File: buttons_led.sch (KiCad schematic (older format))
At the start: 13 parts, among them Q1201 2N7002P, SW1201 SW_Push, SW1202 SW_Push, SW1203 SW_Push, SW1204 SW_Push, SW1205 SW_Push

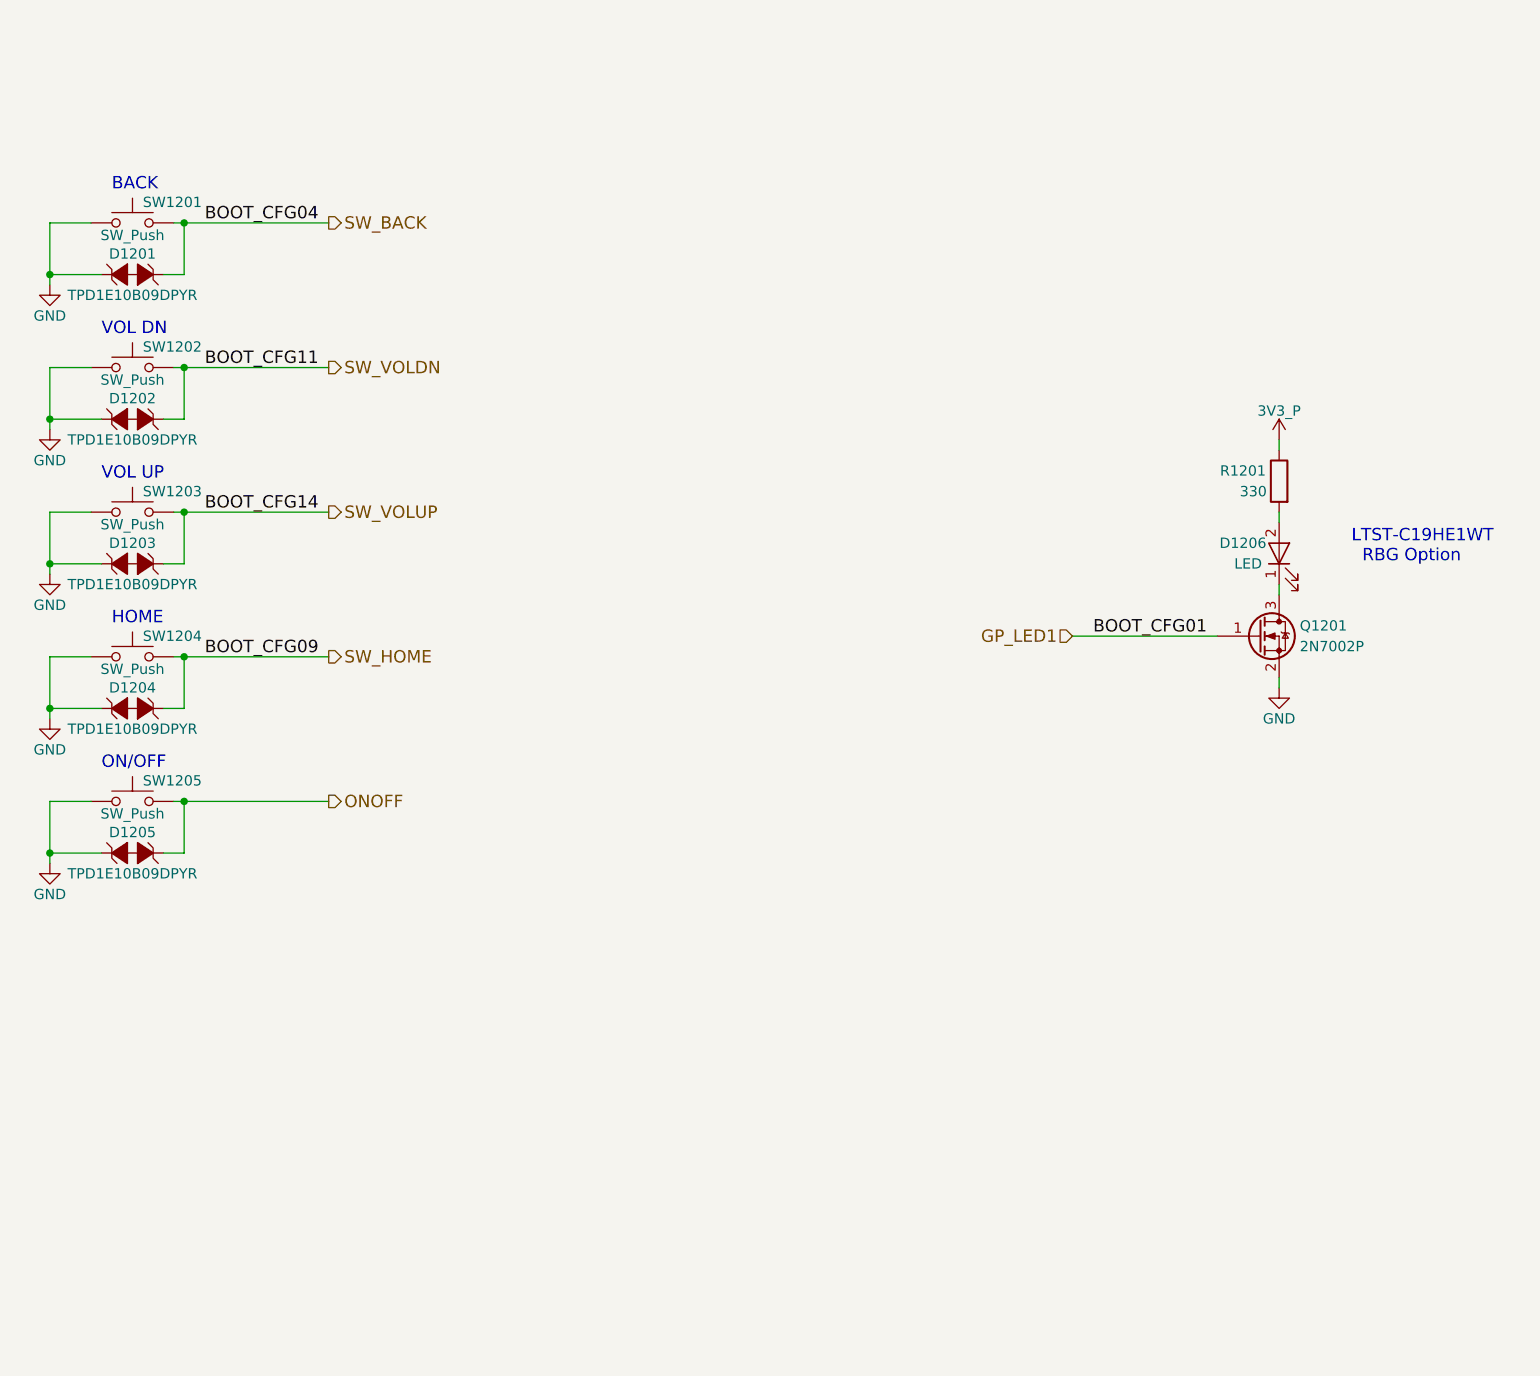
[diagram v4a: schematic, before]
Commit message: Add USB type C circuit with DRP PD capability, should sink near 2A @ 5-6.5V and source 550mA @ 5V
Removed the reverse current protection circuit from the last commit due to the requirement changing to only 18650 battery and USB-C being possible power sources

Next thing to add is the charging circuit when the USB-C is in sink mode/role
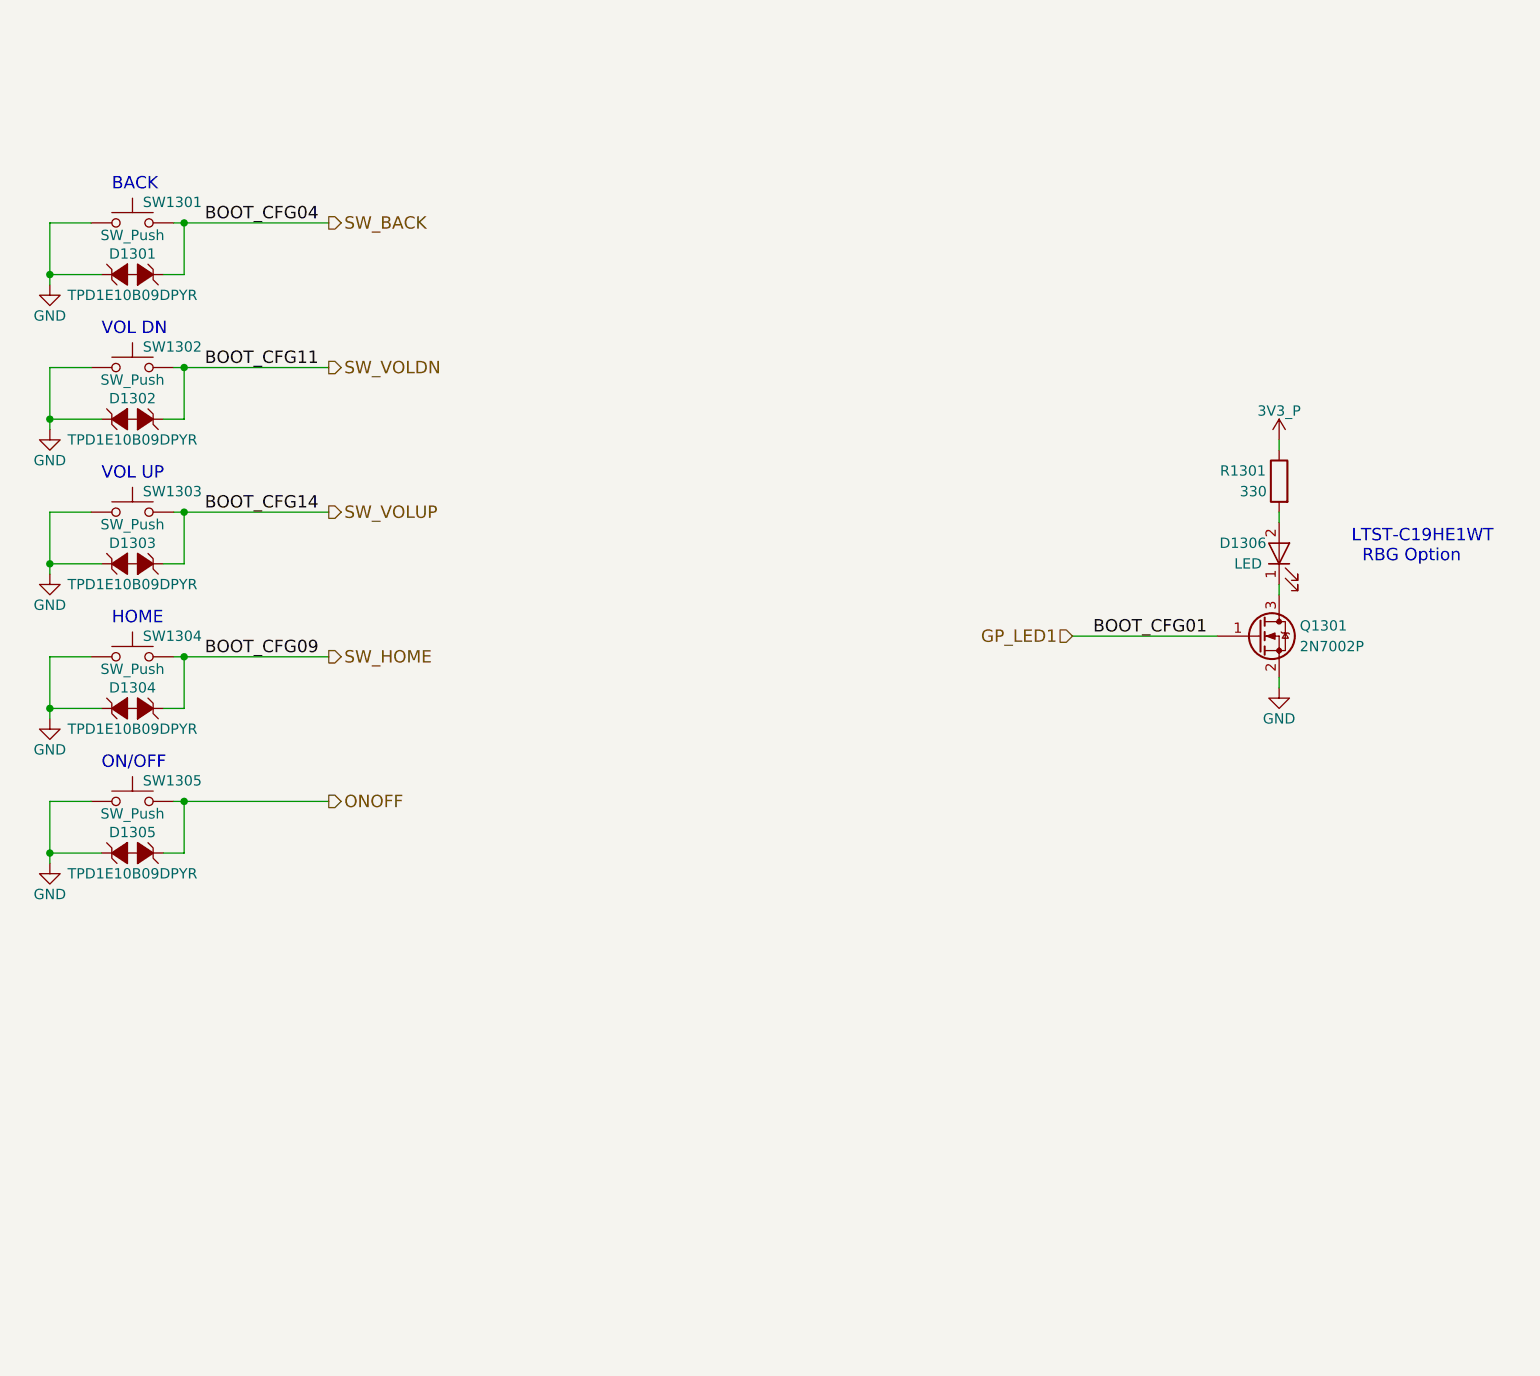
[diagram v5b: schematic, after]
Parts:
- renumbered D1201 to D1301, D1202 to D1302, D1203 to D1303, D1204 to D1304, D1205 to D1305, D1206 to D1306, Q1201 to Q1301, R1201 to R1301, SW1201 to SW1301, SW1202 to SW1302, SW1203 to SW1303, SW1204 to SW1304, SW1205 to SW1305
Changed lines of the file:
@@
 $Descr A4 11693 8268
 encoding utf-8
-Sheet 12 14
+Sheet 13 15
 Title "Buttons & LED"
-Date "2018-04-18"
+Date "2018-04-19"
 Rev "v0.1.0"
 Comp "Purism SPC"
@@
 $EndDescr
 $Comp
-L SW_Push SW1201
+L SW_Push SW1301
 U 1 1 5ACC398C
 P 3200 1700
-F 0 "SW1201" H 3250 1800 50  0000 L CNN
+F 0 "SW1301" H 3250 1800 50  0000 L CNN
 F 1 "SW_Push" H 3200 1640 50  0000 C CNN
 F 2 "" H 3200 1900 50  0001 C CNN
@@
 $EndComp
 $Comp
-L SW_Push SW1202
+L SW_Push SW1302
 U 1 1 5ACC39A6
 P 3200 2400
-F 0 "SW1202" H 3250 2500 50  0000 L CNN
+F 0 "SW1302" H 3250 2500 50  0000 L CNN
 F 1 "SW_Push" H 3200 2340 50  0000 C CNN
 F 2 "" H 3200 2600 50  0001 C CNN
@@
 $EndComp
 $Comp
-L SW_Push SW1203
+L SW_Push SW1303
 U 1 1 5ACC3A06
 P 3200 3100
-F 0 "SW1203" H 3250 3200 50  0000 L CNN
+F 0 "SW1303" H 3250 3200 50  0000 L CNN
 F 1 "SW_Push" H 3200 3040 50  0000 C CNN
 F 2 "" H 3200 3300 50  0001 C CNN
@@
 $EndComp
 $Comp
-L SW_Push SW1204
+L SW_Push SW1304
 U 1 1 5ACC3A3E
 P 3200 3800
-F 0 "SW1204" H 3250 3900 50  0000 L CNN
+F 0 "SW1304" H 3250 3900 50  0000 L CNN
 F 1 "SW_Push" H 3200 3740 50  0000 C CNN
 F 2 "" H 3200 4000 50  0001 C CNN
@@
 $EndComp
 $Comp
-L SW_Push SW1205
+L SW_Push SW1305
 U 1 1 5ACC3AC2
 P 3200 4500
-F 0 "SW1205" H 3250 4600 50  0000 L CNN
+F 0 "SW1305" H 3250 4600 50  0000 L CNN
 F 1 "SW_Push" H 3200 4440 50  0000 C CNN
 F 2 "" H 3200 4700 50  0001 C CNN
@@
 $EndComp
 $Comp
-L TVS_DIODE D1201
+L TVS_DIODE D1301
 U 1 1 5ACC3B61
 P 3200 1950
-F 0 "D1201" H 3200 2050 50  0000 C CNN
+F 0 "D1301" H 3200 2050 50  0000 C CNN
 F 1 "TPD1E10B09DPYR" H 3200 1850 50  0000 C CNN
 F 2 "" H 3300 1950 50  0001 C CNN
@@
 $EndComp
 $Comp
-L TVS_DIODE D1202
+L TVS_DIODE D1302
 U 1 1 5ACC3BD8
 P 3200 2650
-F 0 "D1202" H 3200 2750 50  0000 C CNN
+F 0 "D1302" H 3200 2750 50  0000 C CNN
 F 1 "TPD1E10B09DPYR" H 3200 2550 50  0000 C CNN
 F 2 "" H 3300 2650 50  0001 C CNN
@@
 $EndComp
 $Comp
-L TVS_DIODE D1203
+L TVS_DIODE D1303
 U 1 1 5ACC3D42
 P 3200 3350
-F 0 "D1203" H 3200 3450 50  0000 C CNN
+F 0 "D1303" H 3200 3450 50  0000 C CNN
 F 1 "TPD1E10B09DPYR" H 3200 3250 50  0000 C CNN
 F 2 "" H 3300 3350 50  0001 C CNN
@@
 $EndComp
 $Comp
-L TVS_DIODE D1204
+L TVS_DIODE D1304
 U 1 1 5ACC3EAF
 P 3200 4050
-F 0 "D1204" H 3200 4150 50  0000 C CNN
+F 0 "D1304" H 3200 4150 50  0000 C CNN
 F 1 "TPD1E10B09DPYR" H 3200 3950 50  0000 C CNN
 F 2 "" H 3300 4050 50  0001 C CNN
@@
 $EndComp
 $Comp
-L TVS_DIODE D1205
+L TVS_DIODE D1305
 U 1 1 5ACC3FE9
 P 3200 4750
-F 0 "D1205" H 3200 4850 50  0000 C CNN
+F 0 "D1305" H 3200 4850 50  0000 C CNN
 F 1 "TPD1E10B09DPYR" H 3200 4650 50  0000 C CNN
 F 2 "" H 3300 4750 50  0001 C CNN
@@
 	2800 1700 3000 1700
 $Comp
-L GND #PWR0153
+L GND #PWR0184
 U 1 1 5ACC4A3B
 P 2800 2000
-F 0 "#PWR0153" H 2800 1750 50  0001 C CNN
+F 0 "#PWR0184" H 2800 1750 50  0001 C CNN
 F 1 "GND" H 2800 1850 50  0000 C CNN
 F 2 "" H 2800 2000 50  0001 C CNN
@@
 	2800 2400 3000 2400
 $Comp
-L GND #PWR0154
+L GND #PWR0185
 U 1 1 5ACC4CAE
 P 2800 2700
-F 0 "#PWR0154" H 2800 2450 50  0001 C CNN
+F 0 "#PWR0185" H 2800 2450 50  0001 C CNN
 F 1 "GND" H 2800 2550 50  0000 C CNN
 F 2 "" H 2800 2700 50  0001 C CNN
@@
 	2800 3100 3000 3100
 $Comp
-L GND #PWR0155
+L GND #PWR0186
 U 1 1 5ACC4CDD
 P 2800 3400
-F 0 "#PWR0155" H 2800 3150 50  0001 C CNN
+F 0 "#PWR0186" H 2800 3150 50  0001 C CNN
 F 1 "GND" H 2800 3250 50  0000 C CNN
 F 2 "" H 2800 3400 50  0001 C CNN
@@
 	2800 3800 3000 3800
 $Comp
-L GND #PWR0156
+L GND #PWR0187
 U 1 1 5ACC4E99
 P 2800 4100
-F 0 "#PWR0156" H 2800 3850 50  0001 C CNN
+F 0 "#PWR0187" H 2800 3850 50  0001 C CNN
 F 1 "GND" H 2800 3950 50  0000 C CNN
 F 2 "" H 2800 4100 50  0001 C CNN
@@
 	2800 4500 3000 4500
 $Comp
-L GND #PWR0157
+L GND #PWR0188
 U 1 1 5ACC4EB3
 P 2800 4800
-F 0 "#PWR0157" H 2800 4550 50  0001 C CNN
+F 0 "#PWR0188" H 2800 4550 50  0001 C CNN
 F 1 "GND" H 2800 4650 50  0000 C CNN
 F 2 "" H 2800 4800 50  0001 C CNN
@@
 Connection ~ 3450 4500
 $Comp
-L LED D1206
+L LED D1306
 U 1 1 5ACC7C6F
 P 8750 3300
-F 0 "D1206" V 8800 3475 50  0000 C CNN
+F 0 "D1306" V 8800 3475 50  0000 C CNN
 F 1 "LED" V 8700 3450 50  0000 C CNN
 F 2 "" H 8750 3300 50  0001 C CNN
@@
 $EndComp
 $Comp
-L Q_NMOS_GSD Q1201
+L Q_NMOS_GSD Q1301
 U 1 1 5ACC7CF3
 P 8650 3700
-F 0 "Q1201" H 8850 3750 50  0000 L CNN
+F 0 "Q1301" H 8850 3750 50  0000 L CNN
 F 1 "2N7002P" H 8850 3650 50  0000 L CNN
 F 2 "" H 8850 3800 50  0001 C CNN
@@
 $EndComp
 $Comp
-L GND #PWR0158
+L GND #PWR0189
 U 1 1 5ACC7D2C
 P 8750 3950
-F 0 "#PWR0158" H 8750 3700 50  0001 C CNN
+F 0 "#PWR0189" H 8750 3700 50  0001 C CNN
 F 1 "GND" H 8750 3800 50  0000 C CNN
 F 2 "" H 8750 3950 50  0001 C CNN
@@
 $EndComp
 $Comp
-L R R1201
+L R R1301
 U 1 1 5ACC7E2E
 P 8750 2950
-F 0 "R1201" H 8925 3000 50  0000 C CNN
+F 0 "R1301" H 8925 3000 50  0000 C CNN
 F 1 "330" H 8875 2900 50  0000 C CNN
 F 2 "" V 8680 2950 50  0001 C CNN
@@
 LTST-C19HE1WT\n  RBG Option
 $Comp
-L 3V3_P #PWR0159
+L 3V3_P #PWR0190
 U 1 1 5AEA32FD
 P 8750 2750
-F 0 "#PWR0159" H 8750 2600 50  0001 C CNN
+F 0 "#PWR0190" H 8750 2600 50  0001 C CNN
 F 1 "3V3_P" H 8750 2890 50  0000 C CNN
 F 2 "" H 8750 2750 50  0001 C CNN
